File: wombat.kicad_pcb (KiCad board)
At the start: 2 copper layers, 253.5 x 77.4 mm, 193 parts, among them J1 Conn_01x05, Q1 FDS6630A, SW1 SW_SPST, SW10 SW_SPST, SW101 RESET, SW11 SW_SPST, SW12 SW_SPST, SW13 SW_SPST, SW14 SW_SPST, SW15 SW_SPST, SW16 SW_SPST, SW17 SW_SPST, SW18 SW_SPST, SW19 SW_SPST, SW2 SW_SPST, SW20 SW_SPST, SW21 SW_SPST, SW22 SW_SPST, SW23 SW_SPST, SW24 SW_SPST, SW25 SW_SPST, SW26 SW_SPST, SW27 SW_SPST, SW28 SW_SPST, SW29 SW_SPST, SW3 SW_SPST, SW30 SW_SPST, SW31 SW_SPST, SW32 SW_SPST, SW33 SW_SPST, SW34 SW_SPST, SW35 SW_SPST, SW36 SW_SPST, SW37 SW_SPST, SW38 SW_SPST, SW39 SW_SPST, SW4 SW_SPST, SW40 SW_SPST, SW41 SW_SPST, SW42 SW_SPST, SW43 SW_SPST, SW44 SW_SPST, SW45 SW_SPST, SW46 SW_SPST, SW47 SW_SPST, SW48 SW_SPST, SW49 SW_SPST, SW5 SW_SPST, SW50 SW_SPST, SW51 SW_SPST, SW52 SW_SPST, SW6 SW_SPST, SW7 SW_SPST, SW8 SW_SPST, SW9 SW_SPST, U1 ProMicro

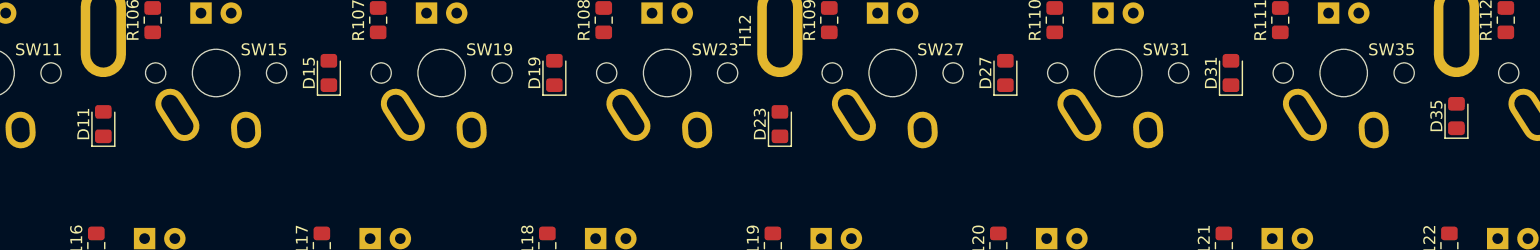
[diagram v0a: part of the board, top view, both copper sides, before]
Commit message: vertically align diodes on top row
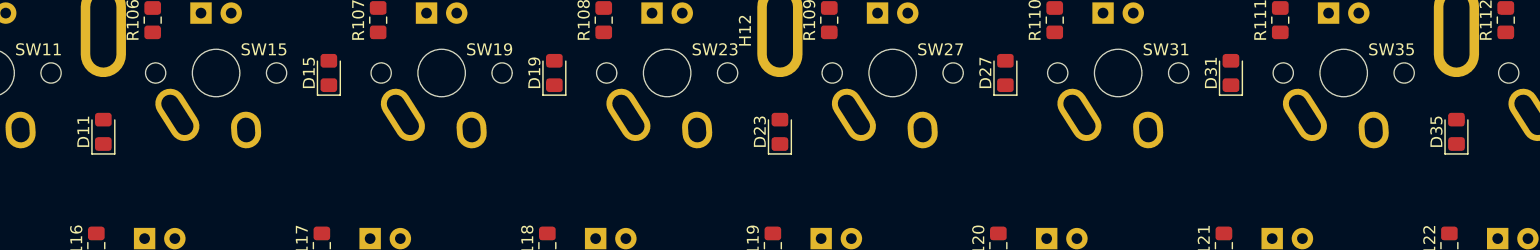
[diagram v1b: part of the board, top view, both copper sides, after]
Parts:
- moved D35 1.32 mm to (231.5, 76.9)
- moved D11 0.65 mm to (117.8, 76.9)
- moved D23 0.65 mm to (174.7, 76.9)
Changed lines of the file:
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@@
   )
   (module Diode_SMD:D_0805_2012Metric_Pad1.15x1.40mm_HandSolder (layer F.Cu)
-    (at 117.836 76.2382 90)
+    (at 117.836 76.8882 90)
     (descr "Diode SMD 0805 (2012 Metric), square (rectangular) end terminal, IPC_7351 nominal, (Body size source: https://docs.google.com/spreadsheets/d/1BsfQQcO9C6DZCsRaXUlFlo91Tg2WpOkGARC1WS5S8t0/edit?usp=sharing), generated with kicad-footprint-generator")
     (tags "diode handsolder")
@@
   )
   (module Diode_SMD:D_0805_2012Metric_Pad1.15x1.40mm_HandSolder (layer F.Cu)
-    (at 231.526 75.5642 90)
+    (at 231.526 76.8882 90)
     (descr "Diode SMD 0805 (2012 Metric), square (rectangular) end terminal, IPC_7351 nominal, (Body size source: https://docs.google.com/spreadsheets/d/1BsfQQcO9C6DZCsRaXUlFlo91Tg2WpOkGARC1WS5S8t0/edit?usp=sharing), generated with kicad-footprint-generator")
     (tags "diode handsolder")
@@
   )
   (module Diode_SMD:D_0805_2012Metric_Pad1.15x1.40mm_HandSolder (layer F.Cu)
-    (at 174.681 76.2382 90)
+    (at 174.681 76.8882 90)
     (descr "Diode SMD 0805 (2012 Metric), square (rectangular) end terminal, IPC_7351 nominal, (Body size source: https://docs.google.com/spreadsheets/d/1BsfQQcO9C6DZCsRaXUlFlo91Tg2WpOkGARC1WS5S8t0/edit?usp=sharing), generated with kicad-footprint-generator")
     (tags "diode handsolder")

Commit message: route traces
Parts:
- added H105: Mouse_Bite, wombat.pretty:Mouse_Bite_04MM_06, F.Cu at (22.7, 135.6)
- added H106: Mouse_Bite, wombat.pretty:Mouse_Bite_04MM_06, F.Cu at (22.7, 118.4)
- H101, H102, H103, H104: footprint wombat.pretty:Mouse_Bite_04MM -> wombat.pretty:Mouse_Bite_04MM_11
- moved R154 4.19 mm to (250.5, 68.1)
- moved D44 0.65 mm to (266.2, 93.6)
- moved D43 0.59 mm to (266.2, 87.2)
- moved D46 0.59 mm to (266.5, 128.8)
- turned R1 to 90 degrees
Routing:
- net Net-(D101-Pad1): track 0.00 -> 659.4 mm, vias 0 -> 3
- net +5V: track 0.00 -> 645.9 mm, vias 0 -> 3
- net /row_3: track 0.00 -> 321.0 mm, vias 0 -> 1
- net /col_4: track 0.00 -> 314.1 mm, vias 0 -> 3
- net /row_2: track 0.00 -> 297.3 mm, vias 0 -> 1
- net /row_0: track 0.00 -> 274.2 mm
- net /col_5: track 0.00 -> 274.1 mm, vias 0 -> 2
- net /row_1: track 0.00 -> 270.8 mm, vias 0 -> 1
- net /col_3: track 0.25 -> 266.9 mm, vias 0 -> 1
- net /col_1: track 0.00 -> 254.2 mm, vias 0 -> 1
- net /LED_CAPSLOCK: track 0.00 -> 238.0 mm, vias 0 -> 3
- net /col_2: track 0.00 -> 237.0 mm, vias 0 -> 1
- net /col_7: track 0.00 -> 219.9 mm, vias 0 -> 1
- net /col_6: track 0.00 -> 218.9 mm, vias 0 -> 3
- net GND: track 0.00 -> 189.5 mm, vias 0 -> 9
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- removed copper zone on B.Cu, net (none)
- removed copper zone on F.Cu, net (none)
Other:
- net class Power: trace_width 0.4 -> 0.35
- board text added: "designed by Eli Gladman"
- board text removed: "haphazardly designed by Eli Gladman"

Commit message: clean up autorouted traces
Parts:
- moved G1 93.4 mm to (32.9, 101.0)
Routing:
- net /col_7: track 219.9 -> 226.9 mm
- net Net-(D34-Pad2): track 33.7 -> 30.9 mm
- net /col_8: track 186.4 -> 184.0 mm
- net Net-(D14-Pad2): track 25.0 -> 22.7 mm
- net /col_5: track 274.1 -> 272.5 mm
- net GND: track 189.5 -> 190.3 mm
- net Net-(D12-Pad2): track 15.4 -> 14.6 mm
- net Net-(D13-Pad2): track 15.4 -> 14.6 mm
- net Net-(D23-Pad2): track 14.5 -> 13.7 mm
- net Net-(D1-Pad2): track 14.5 -> 13.7 mm
- net Net-(D35-Pad2): track 14.5 -> 13.7 mm
- net /col_1: track 254.2 -> 253.5 mm
- net Net-(D11-Pad2): track 14.6 -> 13.8 mm
- net Net-(D2-Pad2): track 15.3 -> 14.6 mm
- net /col_10: track 96.1 -> 95.5 mm
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
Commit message: reposition oshw logo
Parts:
- G1: moved to B.Cu
- moved G1 128.2 mm to (158.1, 128.2), turned to 180 degrees
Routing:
- net GND: track 190.3 -> 181.8 mm
- net /col_1: track 253.5 -> 256.2 mm
- net /col_5: track 272.5 -> 275.1 mm
- net /col_8: track 184.0 -> 183.0 mm
- net /RESET: track 130.1 -> 130.8 mm
- added copper zone on B.Cu, net (none)
- added copper zone on F.Cu, net (none)
